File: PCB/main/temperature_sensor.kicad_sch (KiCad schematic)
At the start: 6 parts, among them Q3 FDS6690A, U7 MCP9700T-ETT

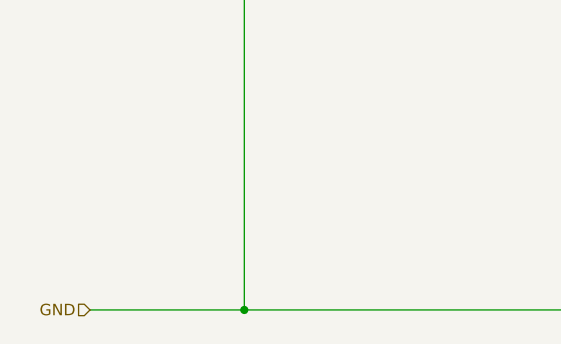
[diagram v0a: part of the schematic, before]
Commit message: Work on reducing ERC flags
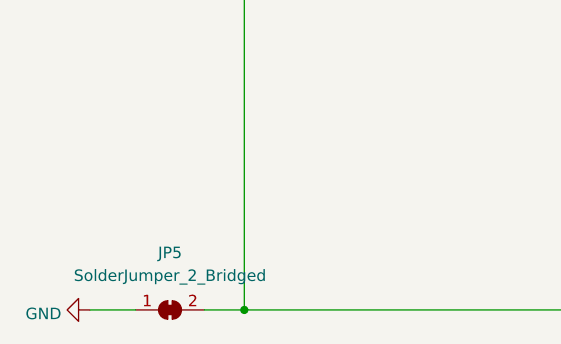
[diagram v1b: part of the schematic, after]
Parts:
- added JP5: SolderJumper_2_Bridged, symbol Jumper:SolderJumper_2_Bridged
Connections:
- net GND: now also JP5.1 (A); no longer D10.1 (K), Q3.1 (S), U7.3 (GND)
- new net: D10.1 (K), JP5.2 (B), Q3.1 (S), U7.3 (GND)
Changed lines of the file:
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@@
     (stroke (width 0) (type default) (color 0 0 0 0))
   )
-  (wire (pts (xy 92.71 135.89) (xy 109.855 135.89))
+  (wire (pts (xy 92.71 135.89) (xy 97.79 135.89))
     (stroke (width 0) (type default) (color 0 0 0 0))
   )
@@
   )
   (wire (pts (xy 109.855 135.89) (xy 165.1 135.89))
+    (stroke (width 0) (type default) (color 0 0 0 0))
+  )
+  (wire (pts (xy 105.41 135.89) (xy 109.855 135.89))
     (stroke (width 0) (type default) (color 0 0 0 0))
   )
@@
     (effects (font (size 1.27 1.27)) (justify left))
   )
-  (hierarchical_label "GND" (shape input) (at 92.71 135.89 180)
-    (effects (font (size 1.27 1.27)) (justify right))
-  )
   (symbol (lib_id "Device:R") (at 186.69 86.36 0) (unit 1)
     (in_bom yes) (on_board yes) (fields_autoplaced)
@@
     (pin "2")
   )
+  (symbol (lib_id "power:GND") (at 92.71 135.89 270) (unit 1)
+    (in_bom yes) (on_board yes) (fields_autoplaced)
+    (property "Reference" "#PWR0102" (id 0) (at 86.36 135.89 0)
+      (effects (font (size 1.27 1.27)) hide)
+    )
+    (property "Value" "GND" (id 1) (at 89.5351 136.3238 90)
+      (effects (font (size 1.27 1.27)) (justify right))
+    )
+    (property "Footprint" "" (id 2) (at 92.71 135.89 0)
+      (effects (font (size 1.27 1.27)) hide)
+    )
+    (property "Datasheet" "" (id 3) (at 92.71 135.89 0)
+      (effects (font (size 1.27 1.27)) hide)
+    )
+    (pin "1")
+  )
   (symbol (lib_id "Symbol_EEE3088F:FDS6690A") (at 102.235 73.66 0) (unit 1)
     (in_bom yes) (on_board yes) (fields_autoplaced)
@@
       (effects (font (size 1.27 1.27)) (justify left) hide)
     )
-    (property "Datasheet" "https://datasheet.lcsc.com/lcsc/1912111437_ON-Semiconductor-FDS6690A_C87667.pdf" (id 3) (at 102.235 55.88 0)
+    (property "Datasheet" "http://www.onsemi.ru.com/pub/Collateral/FDS6690A-D.PDF" (id 3) (at 102.235 55.88 0)
       (effects (font (size 1.27 1.27)) (justify left) hide)
     )
@@
     (pin "8")
   )
+  (symbol (lib_id "Jumper:SolderJumper_2_Bridged") (at 101.6 135.89 0) (unit 1)
+    (in_bom yes) (on_board yes) (fields_autoplaced)
+    (property "Reference" "JP5" (id 0) (at 101.6 129.54 0))
+    (property "Value" "SolderJumper_2_Bridged" (id 1) (at 101.6 132.08 0))
+    (property "Footprint" "" (id 2) (at 101.6 135.89 0)
+      (effects (font (size 1.27 1.27)) hide)
+    )
+    (property "Datasheet" "~" (id 3) (at 101.6 135.89 0)
+      (effects (font (size 1.27 1.27)) hide)
+    )
+    (pin "1")
+    (pin "2")
+  )
 )

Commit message: Add footprints
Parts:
- D10: footprint (none) -> LED_SMD:LED_0603_1608Metric
- JP5: footprint (none) -> Jumper:SolderJumper-2_P1.3mm_Bridged2Bar_Pad1.0x1.5mm
- Q3: footprint ON_Semi-CASE_751EB-0-0-* -> Package_SO:SOIC-8_3.9x4.9mm_P1.27mm
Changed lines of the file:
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@@
       (effects (font (size 1.27 1.27)) (justify right))
     )
-    (property "Footprint" "" (id 2) (at 186.69 99.06 0)
+    (property "Footprint" "LED_SMD:LED_0603_1608Metric" (id 2) (at 186.69 99.06 0)
       (effects (font (size 1.27 1.27)) hide)
     )
@@
       (effects (font (size 1.27 1.27)) (justify left))
     )
-    (property "Footprint" "ON_Semi-CASE_751EB-0-0-*" (id 2) (at 102.235 58.42 0)
+    (property "Footprint" "Package_SO:SOIC-8_3.9x4.9mm_P1.27mm" (id 2) (at 102.235 58.42 0)
       (effects (font (size 1.27 1.27)) (justify left) hide)
     )
@@
     (property "Reference" "JP5" (id 0) (at 101.6 129.54 0))
     (property "Value" "SolderJumper_2_Bridged" (id 1) (at 101.6 132.08 0))
-    (property "Footprint" "" (id 2) (at 101.6 135.89 0)
+    (property "Footprint" "Jumper:SolderJumper-2_P1.3mm_Bridged2Bar_Pad1.0x1.5mm" (id 2) (at 101.6 135.89 0)
       (effects (font (size 1.27 1.27)) hide)
     )

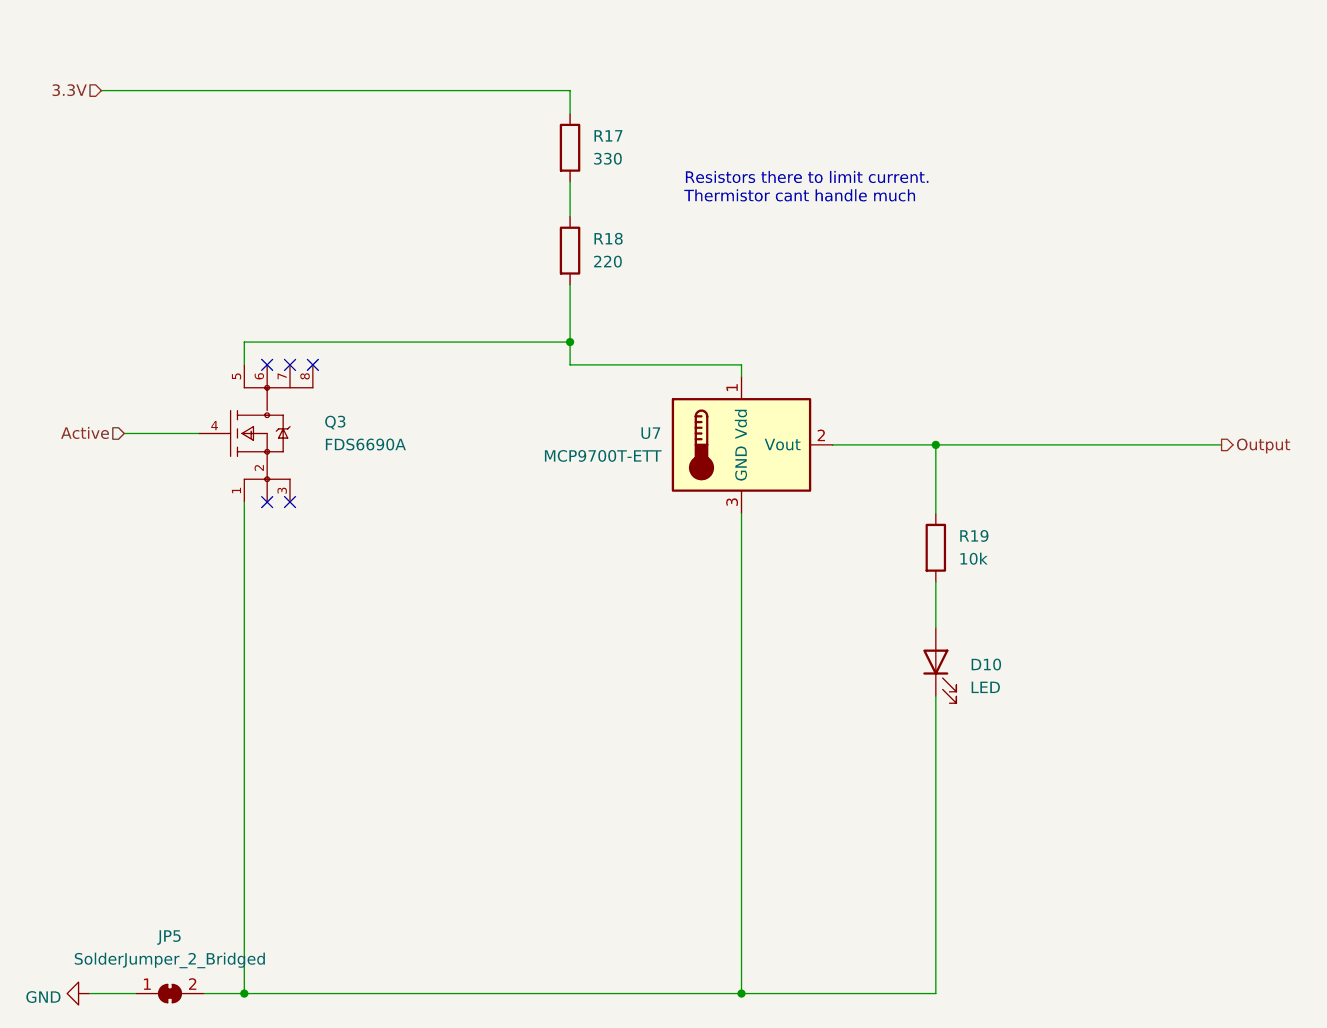
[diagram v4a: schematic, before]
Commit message: Add power flags
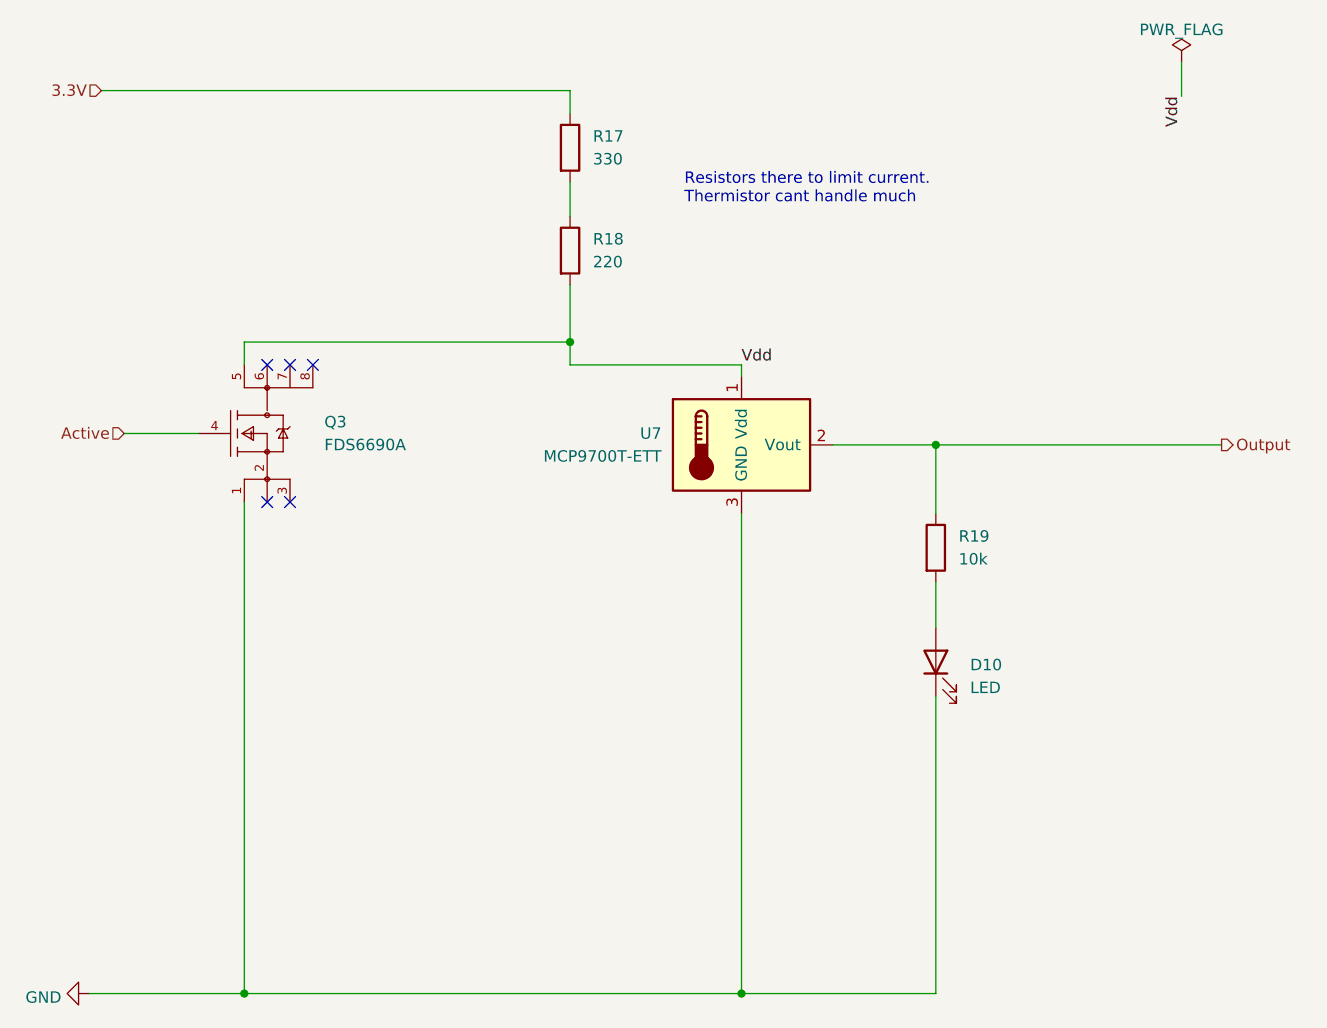
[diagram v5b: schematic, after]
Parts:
- removed JP5: SolderJumper_2_Bridged, Jumper:SolderJumper-2_P1.3mm_Bridged2Bar_Pad1.0x1.5mm, symbol Jumper:SolderJumper_2_Bridged
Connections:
- net GND: now also D10.1 (K), Q3.1 (S), U7.3 (GND)
- net Vdd: now reaches Q3.5 (D), R18.2, U7.1 (Vdd)
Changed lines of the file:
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@@
-    (stroke (width 0) (type default) (color 0 0 0 0))
-  )
-  (wire (pts (xy 92.71 135.89) (xy 97.79 135.89))
     (stroke (width 0) (type default) (color 0 0 0 0))
   )
@@
     (stroke (width 0) (type default) (color 0 0 0 0))
   )
+  (wire (pts (xy 213.995 32.385) (xy 213.995 36.195))
+    (stroke (width 0) (type default) (color 0 0 0 0))
+  )
   (wire (pts (xy 186.69 135.89) (xy 186.69 102.87))
     (stroke (width 0) (type default) (color 0 0 0 0))
@@
     (stroke (width 0) (type default) (color 0 0 0 0))
   )
-  (wire (pts (xy 105.41 135.89) (xy 109.855 135.89))
+  (wire (pts (xy 92.71 135.89) (xy 109.855 135.89))
     (stroke (width 0) (type default) (color 0 0 0 0))
   )
@@
     (effects (font (size 1.27 1.27)) (justify left bottom))
   )
+  (label "Vdd" (at 213.995 36.195 270)
+    (effects (font (size 1.27 1.27)) (justify right bottom))
+  )
+  (label "Vdd" (at 165.1 66.04 0)
+    (effects (font (size 1.27 1.27)) (justify left bottom))
+  )
   (hierarchical_label "Active" (shape input) (at 96.52 73.66 180)
     (effects (font (size 1.27 1.27)) (justify right))
@@
     (pin "1")
     (pin "2")
+  )
+  (symbol (lib_id "power:PWR_FLAG") (at 213.995 32.385 0) (unit 1)
+    (in_bom yes) (on_board yes) (fields_autoplaced)
+    (property "Reference" "#FLG06" (id 0) (at 213.995 30.48 0)
+      (effects (font (size 1.27 1.27)) hide)
+    )
+    (property "Value" "PWR_FLAG" (id 1) (at 213.995 28.8092 0))
+    (property "Footprint" "" (id 2) (at 213.995 32.385 0)
+      (effects (font (size 1.27 1.27)) hide)
+    )
+    (property "Datasheet" "~" (id 3) (at 213.995 32.385 0)
+      (effects (font (size 1.27 1.27)) hide)
+    )
+    (pin "1")
   )
   (symbol (lib_id "Device:R") (at 146.05 53.34 0) (unit 1)
@@
     (pin "8")
   )
-  (symbol (lib_id "Jumper:SolderJumper_2_Bridged") (at 101.6 135.89 0) (unit 1)
-    (in_bom yes) (on_board yes) (fields_autoplaced)
-    (property "Reference" "JP5" (id 0) (at 101.6 129.54 0))
-    (property "Value" "SolderJumper_2_Bridged" (id 1) (at 101.6 132.08 0))
-    (property "Footprint" "Jumper:SolderJumper-2_P1.3mm_Bridged2Bar_Pad1.0x1.5mm" (id 2) (at 101.6 135.89 0)
-      (effects (font (size 1.27 1.27)) hide)
-    )
-    (property "Datasheet" "~" (id 3) (at 101.6 135.89 0)
-      (effects (font (size 1.27 1.27)) hide)
-    )
-    (pin "1")
-    (pin "2")
-  )
 )

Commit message: Add footprints
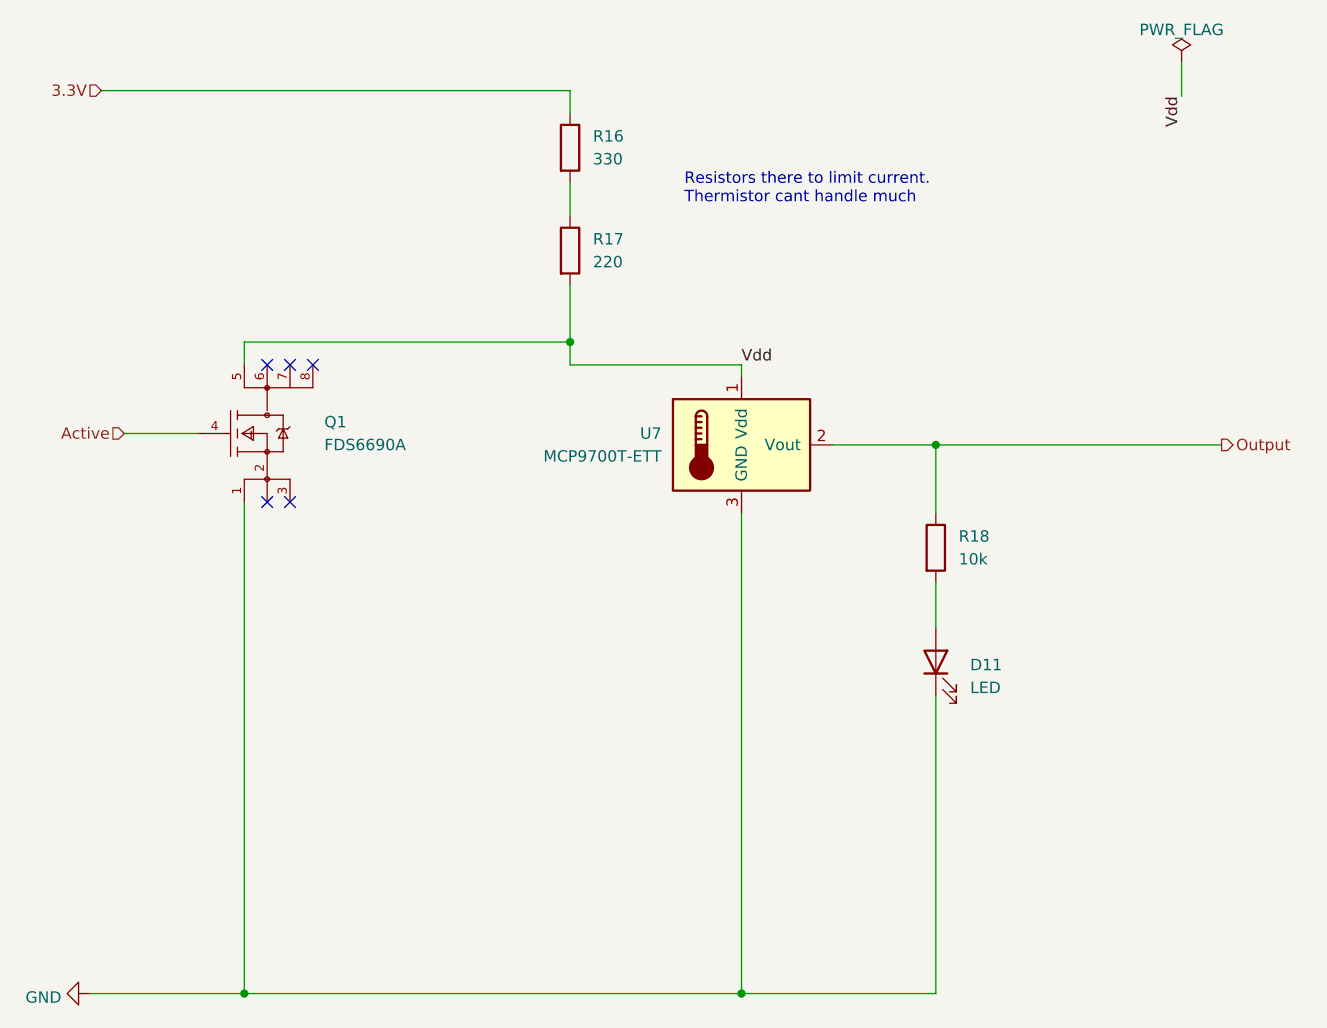
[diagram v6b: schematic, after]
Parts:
- renumbered D10 to D11, Q3 to Q1, R17 to R16, R18 to R17, R19 to R18
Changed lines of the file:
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@@
   (symbol (lib_id "Device:R") (at 186.69 86.36 0) (unit 1)
     (in_bom yes) (on_board yes) (fields_autoplaced)
-    (property "Reference" "R19" (id 0) (at 189.23 85.0899 0)
+    (property "Reference" "R18" (id 0) (at 189.23 85.0899 0)
       (effects (font (size 1.27 1.27)) (justify left))
     )
@@
   (symbol (lib_id "Device:LED") (at 186.69 99.06 90) (unit 1)
     (in_bom yes) (on_board yes) (fields_autoplaced)
-    (property "Reference" "D10" (id 0) (at 190.5 99.3774 90)
+    (property "Reference" "D11" (id 0) (at 190.5 99.3774 90)
       (effects (font (size 1.27 1.27)) (justify right))
     )
@@
   (symbol (lib_id "Device:R") (at 146.05 41.91 0) (unit 1)
     (in_bom yes) (on_board yes) (fields_autoplaced)
-    (property "Reference" "R17" (id 0) (at 148.59 40.6399 0)
+    (property "Reference" "R16" (id 0) (at 148.59 40.6399 0)
       (effects (font (size 1.27 1.27)) (justify left))
     )
@@
   (symbol (lib_id "Device:R") (at 146.05 53.34 0) (unit 1)
     (in_bom yes) (on_board yes) (fields_autoplaced)
-    (property "Reference" "R18" (id 0) (at 148.59 52.0699 0)
+    (property "Reference" "R17" (id 0) (at 148.59 52.0699 0)
       (effects (font (size 1.27 1.27)) (justify left))
     )
@@
   (symbol (lib_id "power:GND") (at 92.71 135.89 270) (unit 1)
     (in_bom yes) (on_board yes) (fields_autoplaced)
-    (property "Reference" "#PWR0102" (id 0) (at 86.36 135.89 0)
+    (property "Reference" "#PWR036" (id 0) (at 86.36 135.89 0)
       (effects (font (size 1.27 1.27)) hide)
     )
@@
   (symbol (lib_id "Symbol_EEE3088F:FDS6690A") (at 102.235 73.66 0) (unit 1)
     (in_bom yes) (on_board yes) (fields_autoplaced)
-    (property "Reference" "Q3" (id 0) (at 118.745 72.3899 0)
+    (property "Reference" "Q1" (id 0) (at 118.745 72.3899 0)
       (effects (font (size 1.27 1.27)) (justify left))
     )

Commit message: Updated BOM
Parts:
- D11: JLC Part # (none) -> C2286; Price (none) -> 0.0032
- Q1: JLC Part # (none) -> C87667; Price (none) -> 0.738
- R16: JLC Part # (none) -> C25104; Price (none) -> 0.0007
- R17: JLC Part # (none) -> C25091; JLCPart C25744 -> (none); Price (none) -> 0.0007
- R18: JLC Part # (none) -> C25744; Price (none) -> 0.0007
- U7: JLC Part # (none) -> C42288; Price (none) -> 0.7397
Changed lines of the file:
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@@
+      (effects (font (size 1.27 1.27)) hide)
+    )
+    (property "JLC Part #" " C25744 " (id 6) (at 186.69 86.36 0)
+      (effects (font (size 1.27 1.27)) hide)
+    )
+    (property "Price" "0.0007" (id 7) (at 186.69 86.36 0)
       (effects (font (size 1.27 1.27)) hide)
     )
@@
       (effects (font (size 1.27 1.27)) hide)
     )
+    (property "JLC Part #" "C2286" (id 5) (at 186.69 99.06 0)
+      (effects (font (size 1.27 1.27)) hide)
+    )
+    (property "Price" "0.0032" (id 6) (at 186.69 99.06 0)
+      (effects (font (size 1.27 1.27)) hide)
+    )
     (pin "1")
     (pin "2")
@@
       (effects (font (size 1.27 1.27)) hide)
     )
+    (property "JLC Part #" " C42288" (id 5) (at 165.1 74.93 0)
+      (effects (font (size 1.27 1.27)) hide)
+    )
+    (property "Price" "0.7397" (id 6) (at 165.1 74.93 0)
+      (effects (font (size 1.27 1.27)) hide)
+    )
     (pin "1")
     (pin "2")
@@
     )
     (property "JLCPart" " C25104" (id 4) (at 146.05 41.91 0)
+      (effects (font (size 1.27 1.27)) hide)
+    )
+    (property "JLC Part #" " C25104" (id 5) (at 146.05 41.91 0)
+      (effects (font (size 1.27 1.27)) hide)
+    )
+    (property "Price" "0.0007" (id 6) (at 146.05 41.91 0)
       (effects (font (size 1.27 1.27)) hide)
     )
@@
       (effects (font (size 1.27 1.27)) hide)
     )
-    (property "JLCPart" " C25744" (id 4) (at 146.05 53.34 0)
+    (property "JLCPart" "" (id 4) (at 146.05 53.34 0)
+      (effects (font (size 1.27 1.27)) hide)
+    )
+    (property "JLC Part #" "C25091" (id 5) (at 146.05 53.34 0)
+      (effects (font (size 1.27 1.27)) hide)
+    )
+    (property "Price" "0.0007" (id 6) (at 146.05 53.34 0)
       (effects (font (size 1.27 1.27)) hide)
     )
@@
       (effects (font (size 1.27 1.27)) hide)
     )
+    (property "JLC Part #" " C87667 " (id 16) (at 102.235 73.66 0)
+      (effects (font (size 1.27 1.27)) hide)
+    )
+    (property "Price" "0.738" (id 17) (at 102.235 73.66 0)
+      (effects (font (size 1.27 1.27)) hide)
+    )

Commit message: Updated BOM
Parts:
- R18: JLC Part # C25744 -> C25744
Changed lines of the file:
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@@
       (effects (font (size 1.27 1.27)) hide)
     )
-    (property "JLC Part #" " C25744 " (id 6) (at 186.69 86.36 0)
+    (property "JLC Part #" "C25744" (id 6) (at 186.69 86.36 0)
       (effects (font (size 1.27 1.27)) hide)
     )
